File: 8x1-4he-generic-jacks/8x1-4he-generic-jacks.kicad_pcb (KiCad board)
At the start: 2 copper layers, 20 x 97.8 mm, 11 parts, among them J1 J1, J10 T, J11 TN1-4, J12 TN5-8, J2 J2, J3 J3, J4 J4, J5 J5, J6 J6, J7 J7, J8 J8

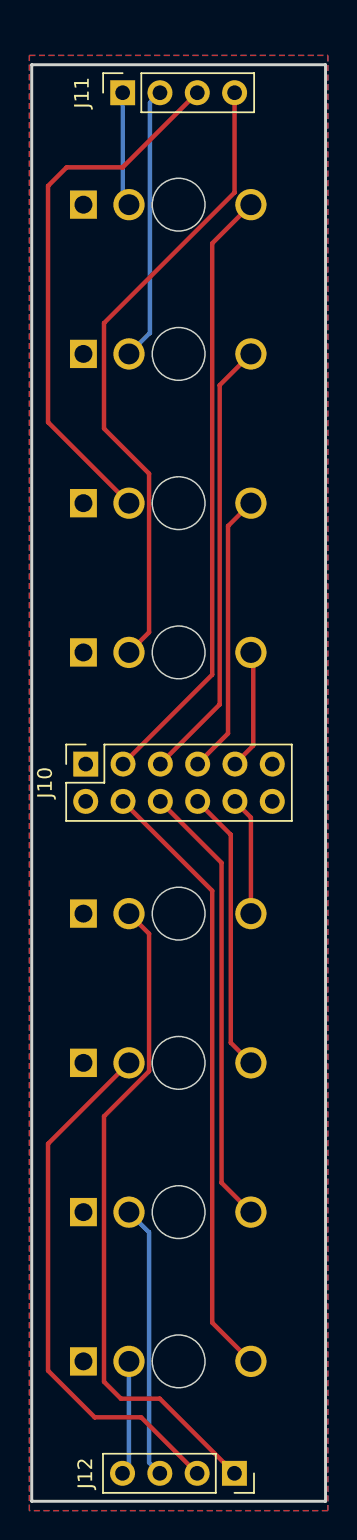
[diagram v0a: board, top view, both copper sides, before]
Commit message: :memo: Add reference text etc to generic-jacks PCB
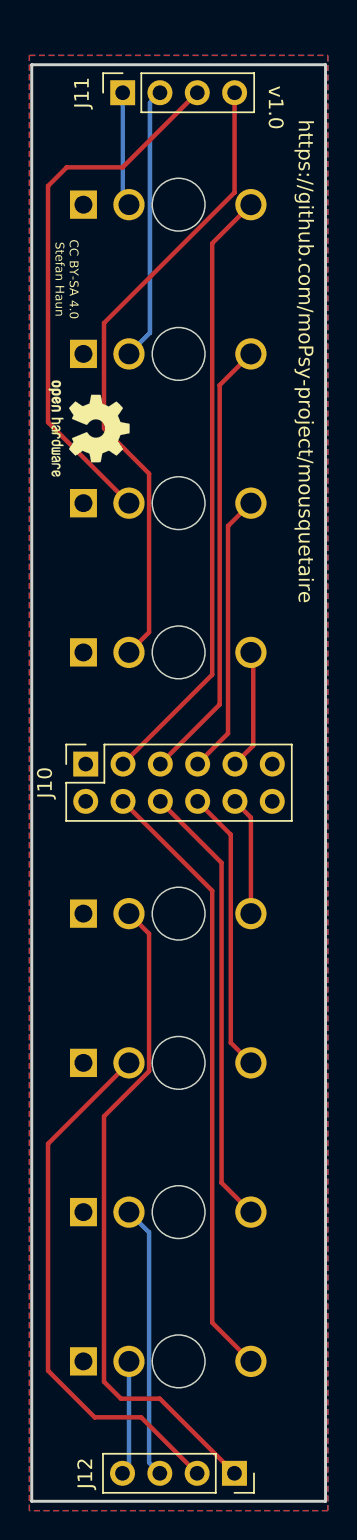
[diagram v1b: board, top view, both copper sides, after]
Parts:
- added REF**: OSHW-Logo2_7.3x6mm_SilkScreen, Symbol:OSHW-Logo2_7.3x6mm_SilkScreen, F.Cu at (120.9, 78.7)
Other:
- board text added: "CC BY-SA 4.0 Stefan Haun"
- board text added: "https://github.com/moPsy-project/mousquetaire"
- board text added: "v1.0"

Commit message: :art: Provide ground to TN connectors
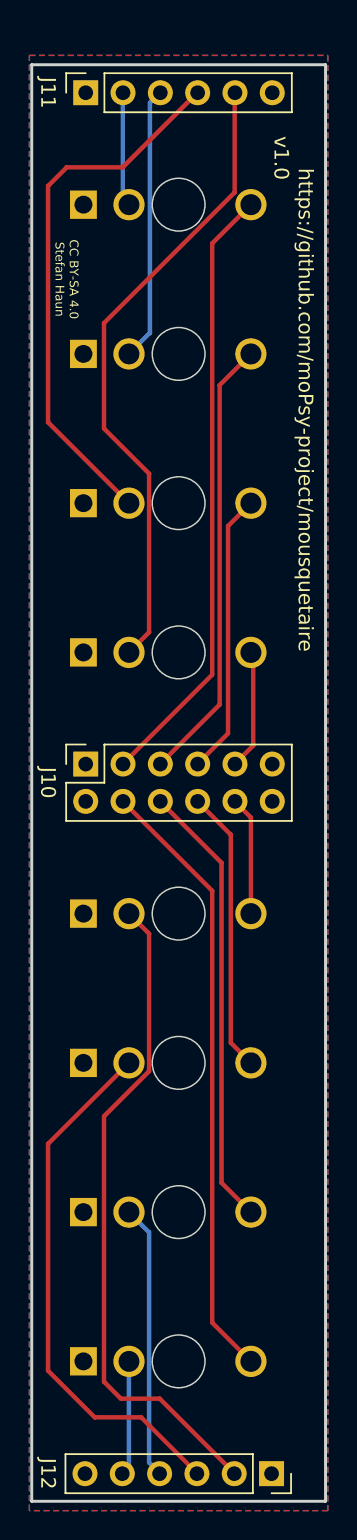
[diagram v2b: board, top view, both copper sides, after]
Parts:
- removed REF**: OSHW-Logo2_7.3x6mm_SilkScreen, Symbol:OSHW-Logo2_7.3x6mm_SilkScreen
- J11, J12: footprint Connector_PinSocket_2.54mm:PinSocket_1x04_P2.54mm_Vertical -> Connector_PinSocket_2.54mm:PinSocket_1x06_P2.54mm_Vertical
- moved J12 2.53 mm to (133.3, 149.9)
- moved J11 2.52 mm to (120.7, 55.9)
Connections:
- J11 pad 1: TN1 -> GND
- J11 pad 2: TN2 -> TN1
- J11 pad 3: TN3 -> TN2
- J11 pad 4: TN4 -> TN3
- J12 pad 1: TN5 -> GND
- J12 pad 2: TN6 -> TN5
- J12 pad 3: TN7 -> TN6
- J12 pad 4: TN8 -> TN7
